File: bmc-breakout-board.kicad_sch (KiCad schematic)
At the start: 5 parts

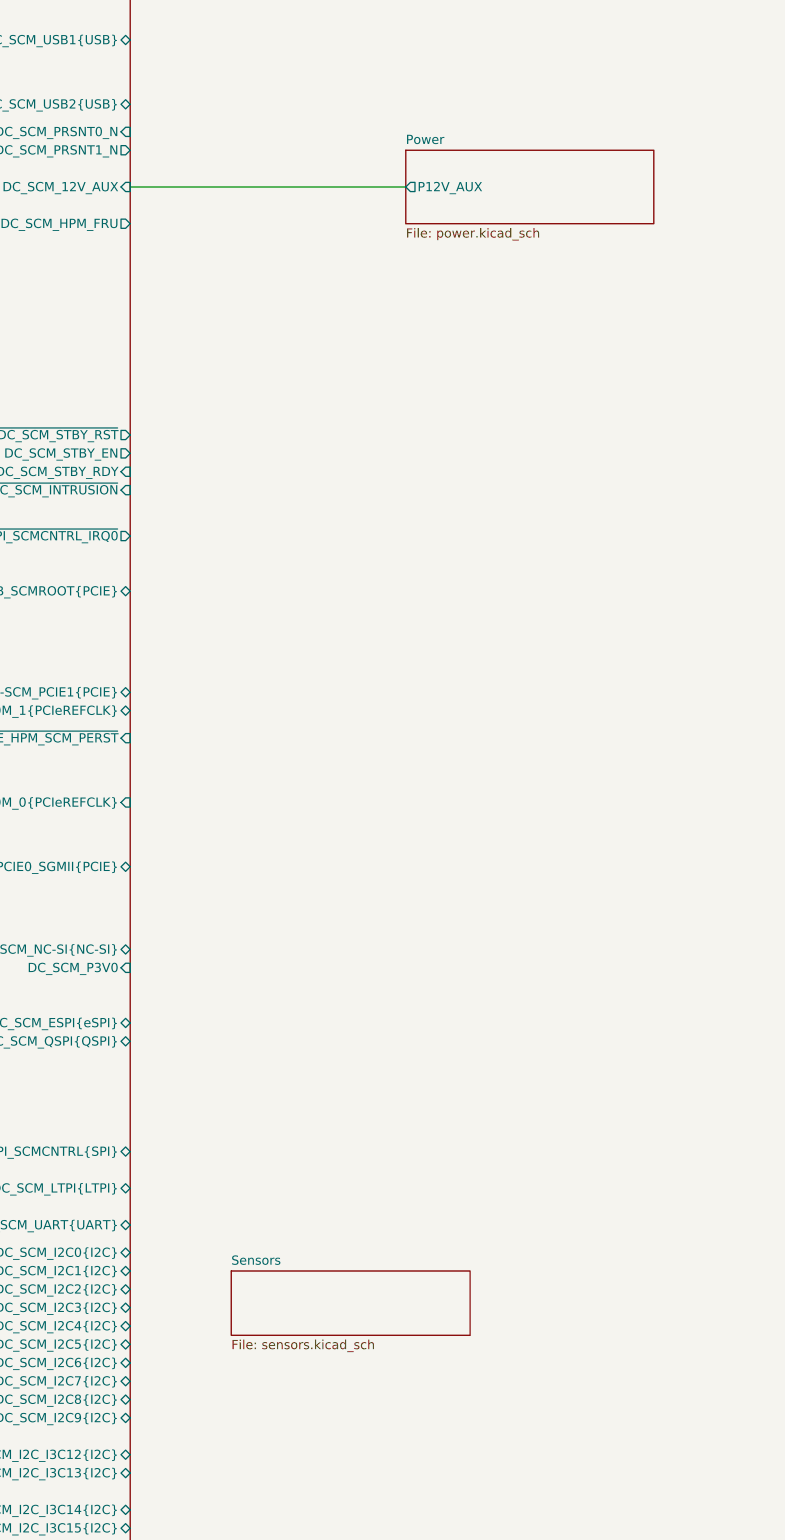
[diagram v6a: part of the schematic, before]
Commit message: [#92504] Add temperature sensor
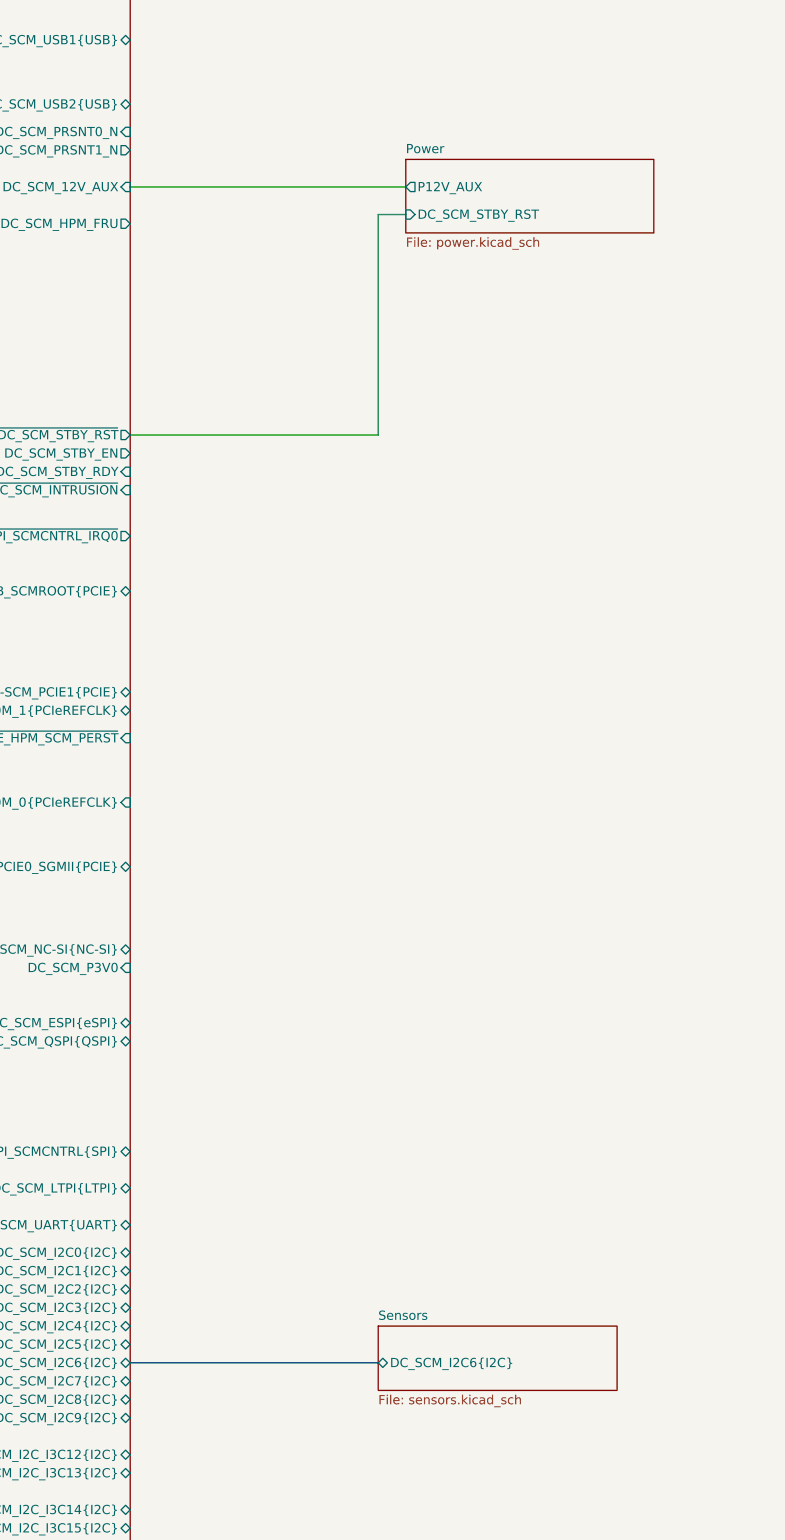
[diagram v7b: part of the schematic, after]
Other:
- sheet Power ports: added DC_SCM_STBY_RST; removed none
- sheet Sensors ports: added DC_SCM_I2C6{I2C}; removed none
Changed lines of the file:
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@@
+		)
+	)
+	(bus
+		(pts
+			(xy 57.15 222.25) (xy 91.44 222.25)
+		)
+		(stroke
+			(width 0)
+			(type default)
+		)
+	)
+	(wire
+		(pts
+			(xy 91.44 93.98) (xy 57.15 93.98)
+		)
+		(stroke
+			(width 0)
+			(type default)
+		)
+	)
+	(wire
+		(pts
+			(xy 95.25 63.5) (xy 91.44 63.5)
+		)
+		(stroke
+			(width 0)
+			(type default)
 		)
 	)
@@
 		(pts
 			(xy 57.15 59.69) (xy 95.25 59.69)
+		)
+		(stroke
+			(width 0)
+			(type default)
+		)
+	)
+	(wire
+		(pts
+			(xy 91.44 63.5) (xy 91.44 93.98)
 		)
 		(stroke
@@
 	)
 	(sheet
-		(at 95.25 54.61)
+		(at 95.25 55.88)
 		(size 34.29 10.16)
 		(exclude_from_sim no)
@@
 		)
 		(property "Sheetname" "Power"
-			(at 95.25 53.8984 0)
+			(at 95.25 55.1684 0)
 			(effects
 				(font
@@
 		)
 		(property "Sheetfile" "power.kicad_sch"
-			(at 95.25 65.3546 0)
+			(at 95.25 66.6246 0)
 			(effects
 				(font
@@
 		(pin "P12V_AUX" output
 			(at 95.25 59.69 180)
+			(effects
+				(font
+					(size 1.27 1.27)
+				)
+				(justify left)
+			)
+		)
+		(pin "DC_SCM_STBY_RST" input
+			(at 95.25 63.5 180)
 			(effects
 				(font
@@
 	)
 	(sheet
-		(at 71.12 209.55)
+		(at 91.44 217.17)
 		(size 33.02 8.89)
 		(exclude_from_sim no)
@@
 		)
 		(property "Sheetname" "Sensors"
-			(at 71.12 208.8384 0)
+			(at 91.44 216.4584 0)
 			(effects
 				(font
@@
 		)
 		(property "Sheetfile" "sensors.kicad_sch"
-			(at 71.12 219.0246 0)
+			(at 91.44 226.6446 0)
 			(effects
 				(font
@@
 			)
 		)
+		(pin "DC_SCM_I2C6{I2C}" bidirectional
+			(at 91.44 222.25 180)
+			(effects
+				(font
+					(size 1.27 1.27)
+				)
+				(justify left)
+			)
+		)

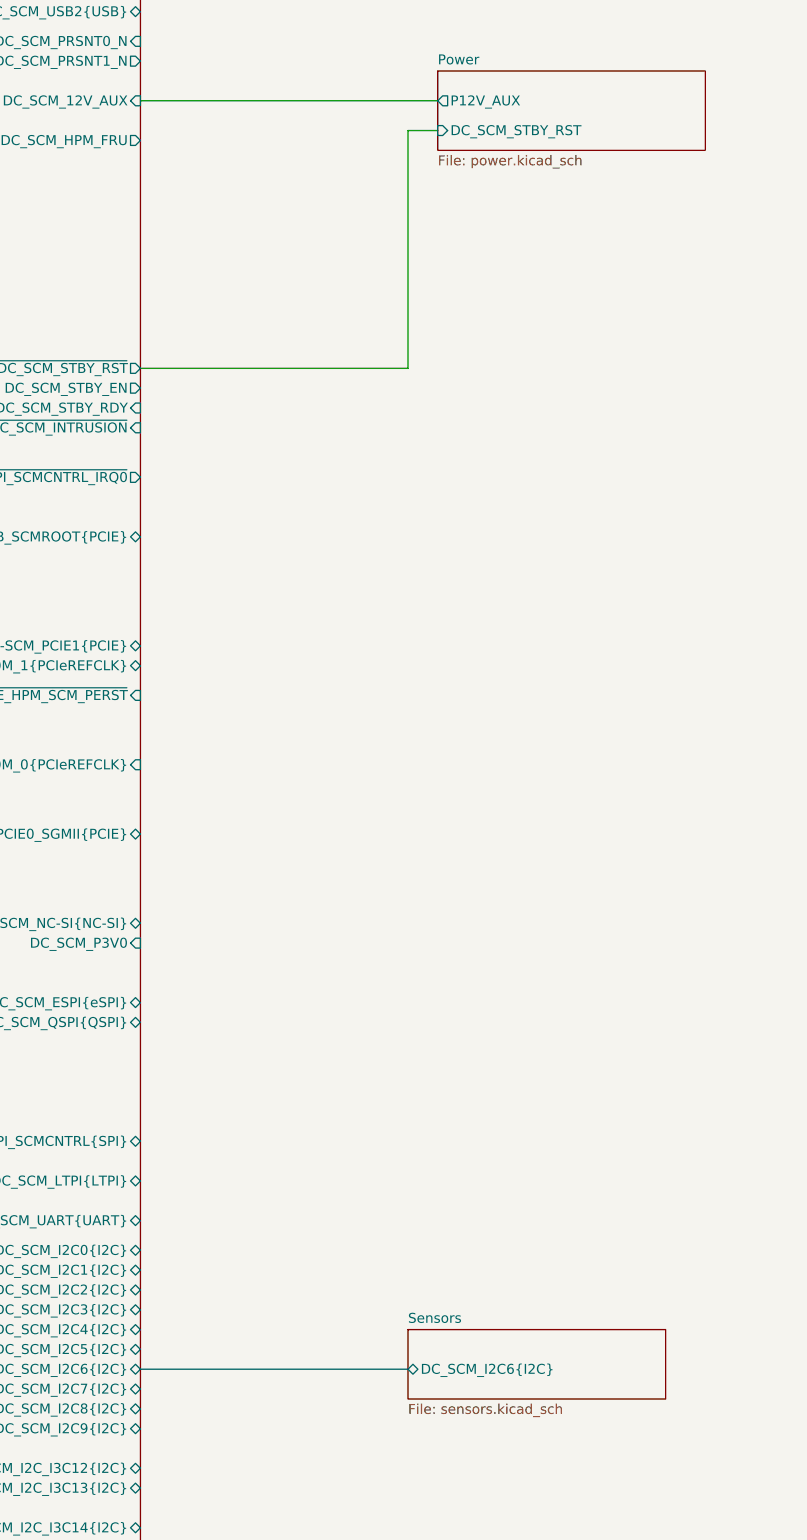
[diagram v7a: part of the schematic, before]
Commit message: [#92504] Add AT24C04C EEPROM
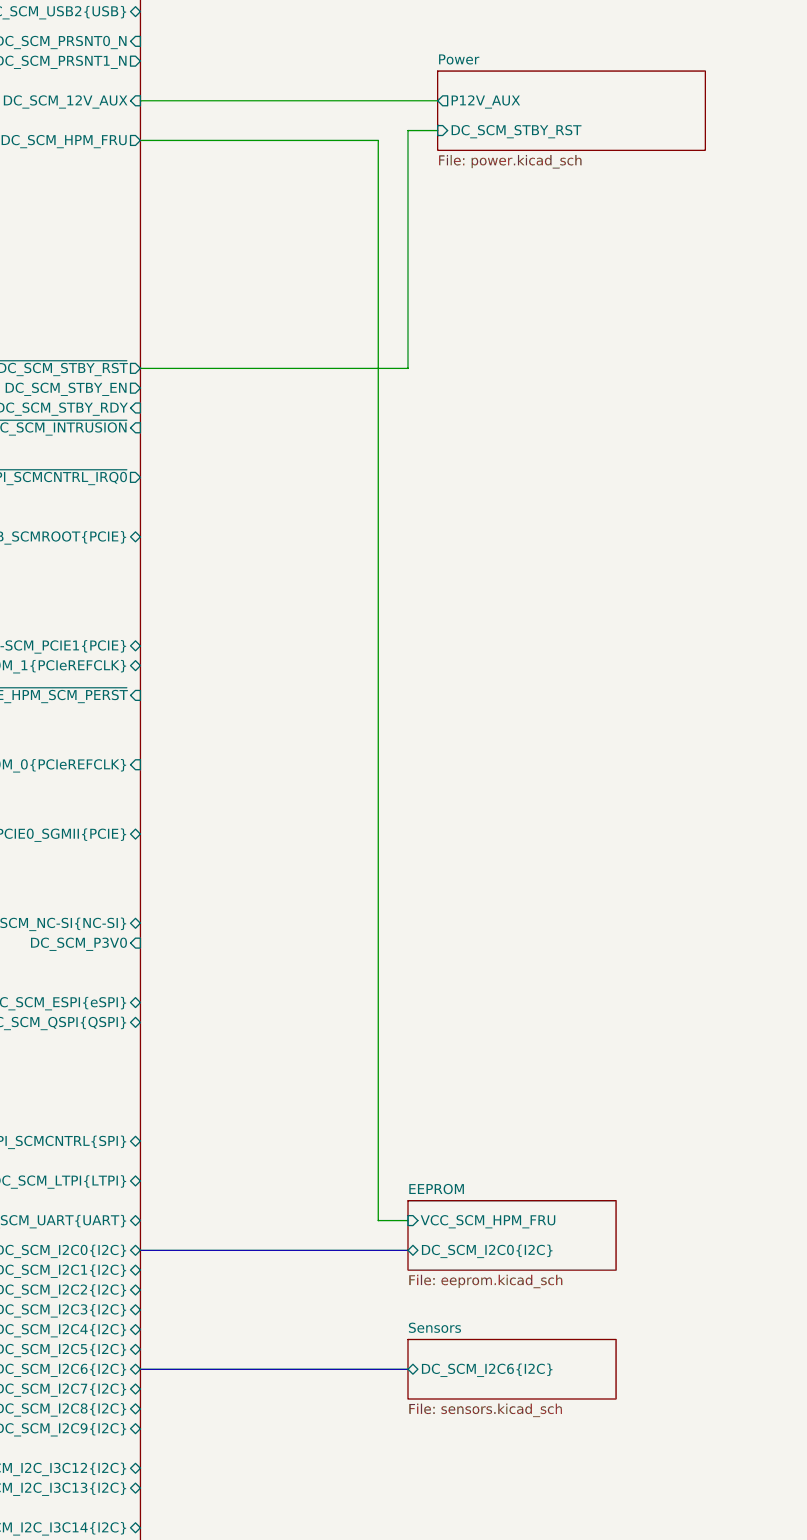
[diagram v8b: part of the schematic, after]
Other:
- added sheet EEPROM (eeprom.kicad_sch)
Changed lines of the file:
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@@
+		)
+	)
+	(bus
+		(pts
+			(xy 57.15 207.01) (xy 91.44 207.01)
+		)
+		(stroke
+			(width 0)
+			(type default)
+		)
+	)
+	(wire
+		(pts
+			(xy 57.15 64.77) (xy 87.63 64.77)
+		)
+		(stroke
+			(width 0)
+			(type default)
+		)
+	)
+	(wire
+		(pts
+			(xy 87.63 203.2) (xy 91.44 203.2)
+		)
+		(stroke
+			(width 0)
+			(type default)
 		)
 	)
@@
 		(pts
 			(xy 95.25 63.5) (xy 91.44 63.5)
+		)
+		(stroke
+			(width 0)
+			(type default)
+		)
+	)
+	(wire
+		(pts
+			(xy 87.63 64.77) (xy 87.63 203.2)
 		)
 		(stroke
@@
 	)
 	(sheet
+		(at 91.44 200.66)
+		(size 26.67 8.89)
+		(exclude_from_sim no)
+		(in_bom yes)
+		(on_board yes)
+		(dnp no)
+		(fields_autoplaced yes)
+		(stroke
+			(width 0.1524)
+			(type solid)
+		)
+		(fill
+			(color 0 0 0 0.0000)
+		)
+		(property "Sheetname" "EEPROM"
+			(at 91.44 199.9484 0)
+			(effects
+				(font
+					(size 1.27 1.27)
+				)
+				(justify left bottom)
+			)
+		)
+		(property "Sheetfile" "eeprom.kicad_sch"
+			(at 91.44 210.1346 0)
+			(effects
+				(font
+					(size 1.27 1.27)
+				)
+				(justify left top)
+			)
+		)
+		(pin "DC_SCM_I2C0{I2C}" bidirectional
+			(at 91.44 207.01 180)
+			(effects
+				(font
+					(size 1.27 1.27)
+				)
+				(justify left)
+			)
+		)
+		(pin "VCC_SCM_HPM_FRU" input
+			(at 91.44 203.2 180)
+			(effects
+				(font
+					(size 1.27 1.27)
+				)
+				(justify left)
+			)
+		)
+		(instances
+			(project "bmc-breakout-board"
+				(path "/5d67ef28-5805-4f87-b722-2926dabf7f6e"
+					(page "5")
+				)
+			)
+		)
+	)
+	(sheet
 		(at 95.25 55.88)
 		(size 34.29 10.16)
@@
 	)
 	(sheet
-		(at 91.44 217.17)
-		(size 33.02 8.89)
+		(at 91.44 218.44)
+		(size 26.67 7.62)
 		(exclude_from_sim no)
 		(in_bom yes)
@@
 		)
 		(property "Sheetname" "Sensors"
-			(at 91.44 216.4584 0)
-			(effects
-				(font
+			(at 91.44 217.7284 0)
+			(effects
+				(font
